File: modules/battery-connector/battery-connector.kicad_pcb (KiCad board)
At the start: 2 copper layers, 15 x 12.7 mm, 2 parts, among them J1 691210910002

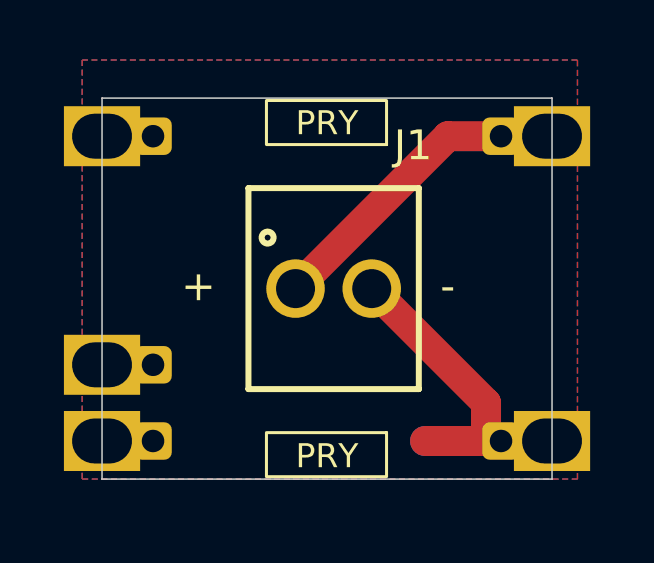
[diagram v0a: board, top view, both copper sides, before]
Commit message: Updating workflow to detect kicad changes
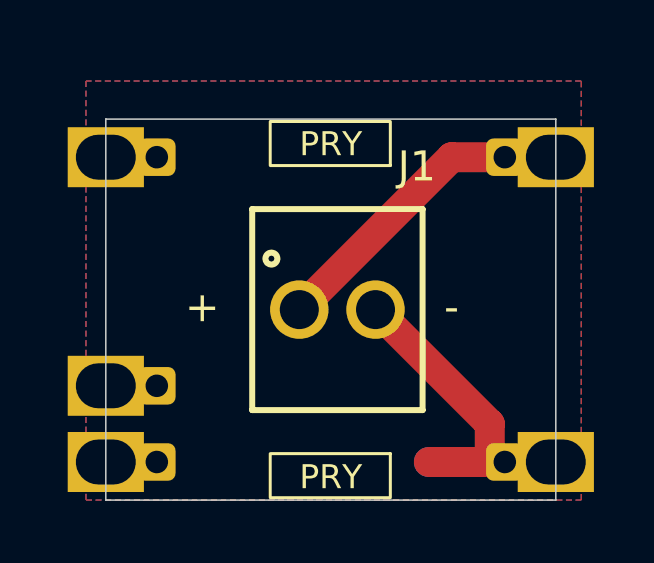
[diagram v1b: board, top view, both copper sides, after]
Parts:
- moved J1 0.71 mm to (68.0, 61.6)
- moved M1 0.71 mm to (67.8, 61.6)
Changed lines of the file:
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@@
 	(footprint "MegaCastle:691210910002"
 		(layer "F.Cu")
-		(at 67.906 60.88)
+		(at 68.032 61.58)
 		(descr "<b>WR-TBL Serie 2109 - 2.54 mm Horiz. Entry<br></b>Max Height =8.5mm , Pitch 2.54mm , 2 Pins")
 		(property "Reference" "J1"
@@
 	(footprint "MegaCastle:MegaCastle2x5-Module-I15.0x7.9-M8CC-SPAREPAD"
 		(layer "B.Cu")
-		(at 67.686 60.88 180)
+		(at 67.812 61.58 180)
 		(property "Reference" "M1"
 			(at -2.948 -5.65 0)
@@
 			(polygon
 				(pts
-					(xy 69.670241 56.078592) (xy 69.670241 54.61) (xy 65.666484 54.61) (xy 65.666484 56.078592)
+					(xy 69.796241 56.778592) (xy 69.796241 55.31) (xy 65.792484 55.31) (xy 65.792484 56.778592)
 				)
 			)
@@
 			(polygon
 				(pts
-					(xy 69.670241 65.681408) (xy 69.670241 67.15) (xy 65.666484 67.15) (xy 65.666484 65.681408)
+					(xy 69.796241 66.381408) (xy 69.796241 67.85) (xy 65.792484 67.85) (xy 65.792484 66.381408)
 				)
 			)
@@
 			(polygon
 				(pts
-					(xy 75.186 54.53) (xy 75.186 56.93) (xy 60.186 56.93) (xy 60.186 54.53)
+					(xy 75.312 55.23) (xy 75.312 57.63) (xy 60.312 57.63) (xy 60.312 55.23)
 				)
 			)
@@
 			(polygon
 				(pts
-					(xy 75.186 67.23) (xy 75.186 64.83) (xy 60.186 64.83) (xy 60.186 67.23)
+					(xy 75.312 67.93) (xy 75.312 65.53) (xy 60.312 65.53) (xy 60.312 67.93)
 				)
 			)
@@
 	)
 	(gr_text "-"
-		(at 71.462 61.388 0)
+		(at 71.588 62.088 0)
 		(layer "F.SilkS")
 		(effects
@@
 	)
 	(gr_text "+"
-		(at 62.826 61.388 0)
+		(at 62.952 62.088 0)
 		(layer "F.SilkS")
 		(effects
@@
 	)
 	(gr_text "R20250405"
-		(at 64.9596 57.6542 90)
+		(at 65.0856 58.3542 90)
 		(layer "B.SilkS")
 		(effects
@@
 	)
 	(segment
-		(start 72.986 55.8)
-		(end 71.716 55.8)
+		(start 73.112 56.5)
+		(end 71.842 56.5)
 		(width 1)
 		(layer "F.Cu")
@@
 	)
 	(segment
-		(start 71.716 55.8)
-		(end 66.636 60.88)
+		(start 71.842 56.5)
+		(end 66.762 61.58)
 		(width 1)
 		(layer "F.Cu")
@@
 	)
 	(segment
-		(start 72.986 65.96)
-		(end 72.986 64.69)
+		(start 73.112 66.66)
+		(end 73.112 65.39)
 		(width 1)
 		(layer "F.Cu")
@@
 	)
 	(segment
-		(start 72.986 64.69)
-		(end 69.176 60.88)
+		(start 73.112 65.39)
+		(end 69.302 61.58)
 		(width 1)
 		(layer "F.Cu")
@@
 	)
 	(segment
-		(start 72.986 65.96)
-		(end 70.954 65.96)
+		(start 73.112 66.66)
+		(end 71.08 66.66)
 		(width 1)
 		(layer "F.Cu")
@@
 	)
 	(segment
-		(start 72.986 65.96)
-		(end 70.954 65.96)
+		(start 73.112 66.66)
+		(end 71.08 66.66)
 		(width 1)
 		(layer "B.Cu")
@@
 		(polygon
 			(pts
-				(xy 59.524 53.26) (xy 59.524 67.23) (xy 76.034 67.23) (xy 76.034 53.26)
-			)
-		)
+				(xy 59.65 53.96) (xy 59.65 67.93) (xy 76.16 67.93) (xy 76.16 53.96)
+			)
+		)

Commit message: Updating all modules
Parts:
- moved J1 0.39 mm to (67.8, 61.3)
- moved M1 0.39 mm to (67.6, 61.3)
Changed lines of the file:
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@@
 	(footprint "MegaCastle:691210910002"
 		(layer "F.Cu")
-		(at 68.032 61.58)
+		(at 67.775 61.285)
 		(descr "<b>WR-TBL Serie 2109 - 2.54 mm Horiz. Entry<br></b>Max Height =8.5mm , Pitch 2.54mm , 2 Pins")
 		(property "Reference" "J1"
@@
 	(footprint "MegaCastle:MegaCastle2x5-Module-I15.0x7.9-M8CC-SPAREPAD"
 		(layer "B.Cu")
-		(at 67.812 61.58 180)
+		(at 67.555 61.285 180)
 		(property "Reference" "M1"
 			(at -2.948 -5.65 0)
@@
 			(polygon
 				(pts
-					(xy 69.796241 56.778592) (xy 69.796241 55.31) (xy 65.792484 55.31) (xy 65.792484 56.778592)
+					(xy 69.539241 56.483592) (xy 69.539241 55.015) (xy 65.535484 55.015) (xy 65.535484 56.483592)
 				)
 			)
@@
 			(polygon
 				(pts
-					(xy 69.796241 66.381408) (xy 69.796241 67.85) (xy 65.792484 67.85) (xy 65.792484 66.381408)
+					(xy 69.539241 66.086408) (xy 69.539241 67.555) (xy 65.535484 67.555) (xy 65.535484 66.086408)
 				)
 			)
@@
 			(polygon
 				(pts
-					(xy 75.312 55.23) (xy 75.312 57.63) (xy 60.312 57.63) (xy 60.312 55.23)
+					(xy 75.055 54.935) (xy 75.055 57.335) (xy 60.055 57.335) (xy 60.055 54.935)
 				)
 			)
@@
 			(polygon
 				(pts
-					(xy 75.312 67.93) (xy 75.312 65.53) (xy 60.312 65.53) (xy 60.312 67.93)
+					(xy 75.055 67.635) (xy 75.055 65.235) (xy 60.055 65.235) (xy 60.055 67.635)
 				)
 			)
@@
 	)
 	(gr_text "-"
-		(at 71.588 62.088 0)
+		(at 71.331 61.793 0)
 		(layer "F.SilkS")
 		(effects
@@
 	)
 	(gr_text "+"
-		(at 62.952 62.088 0)
+		(at 62.695 61.793 0)
 		(layer "F.SilkS")
 		(effects
@@
 	)
 	(gr_text "R20250405"
-		(at 65.0856 58.3542 90)
+		(at 64.8286 58.0592 90)
 		(layer "B.SilkS")
 		(effects
@@
 	)
 	(segment
-		(start 73.112 56.5)
-		(end 71.842 56.5)
+		(start 72.855 56.205)
+		(end 71.585 56.205)
 		(width 1)
 		(layer "F.Cu")
@@
 	)
 	(segment
-		(start 71.842 56.5)
-		(end 66.762 61.58)
+		(start 71.585 56.205)
+		(end 66.505 61.285)
 		(width 1)
 		(layer "F.Cu")
@@
 	)
 	(segment
-		(start 73.112 66.66)
-		(end 73.112 65.39)
+		(start 72.855 66.365)
+		(end 72.855 65.095)
 		(width 1)
 		(layer "F.Cu")
@@
 	)
 	(segment
-		(start 73.112 65.39)
-		(end 69.302 61.58)
+		(start 72.855 65.095)
+		(end 69.045 61.285)
 		(width 1)
 		(layer "F.Cu")
@@
 	)
 	(segment
-		(start 73.112 66.66)
-		(end 71.08 66.66)
+		(start 72.855 66.365)
+		(end 70.823 66.365)
 		(width 1)
 		(layer "F.Cu")
@@
 	)
 	(segment
-		(start 73.112 66.66)
-		(end 71.08 66.66)
+		(start 72.855 66.365)
+		(end 70.823 66.365)
 		(width 1)
 		(layer "B.Cu")
@@
 		(polygon
 			(pts
-				(xy 59.65 53.96) (xy 59.65 67.93) (xy 76.16 67.93) (xy 76.16 53.96)
-			)
-		)
+				(xy 59.393 53.665) (xy 59.393 67.635) (xy 75.903 67.635) (xy 75.903 53.665)
+			)
+		)
